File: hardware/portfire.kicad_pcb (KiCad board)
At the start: 2 copper layers, 100 x 100 mm, 200 parts, among them IC101 STM32F407VGT6TR, IC102 TPS62152, IC103 25AA02E48, IC104 ADP3335, IC105 SNx5176B, IC201 MAX5969x, IC202 KSZ8081RNA, IC203 MAX17503, IC301 TPS92512, J201 RJ45, J202 AUX POWER, P101 SWD_TC, P102 AUX_BUS_RX, P103 AUX_BUS_RX, P301 1, P302 2, P303 3, P304 4, P305 5, P306 6, P307 7, P308 8, P309 9, P310 10, P311 11, P312 12, P313 13, P314 14, P315 15, P316 16, P317 17, P318 18, P319 19, P320 20, P321 21, P322 22, P323 23, P324 24, P325 25, P326 26, P327 27, P328 28, P329 29, P330 30, Q301 NTR4501NT1G, Q302 NTR4501NT1G, Q303 NTR4501NT1G, Q304 NTR4501NT1G, Q305 NTR4501NT1G, Q306 NTR4501NT1G, Q307 NTR4501NT1G, Q308 NTR4501NT1G, Q309 NTR4501NT1G, Q310 NTR4501NT1G, Q311 NTR4501NT1G, Q312 NTR4501NT1G, Q313 NTR4501NT1G, Q314 NTR4501NT1G, Q315 NTR4501NT1G, Q316 NTR4501NT1G, Q317 NTR4501NT1G, Q318 NTR4501NT1G, Q319 NTR4501NT1G, Q320 NTR4501NT1G, Q321 NTR4501NT1G, Q322 NTR4501NT1G, Q323 NTR4501NT1G, Q324 NTR4501NT1G, Q325 NTR4501NT1G, Q326 NTR4501NT1G, Q327 NTR4501NT1G, Q328 NTR4501NT1G, Q329 NTR4501NT1G, Q330 NTR4501NT1G, T201 749010012A, X101 PART, X102 PART, X103 PART, X104 PART, Y101 26M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

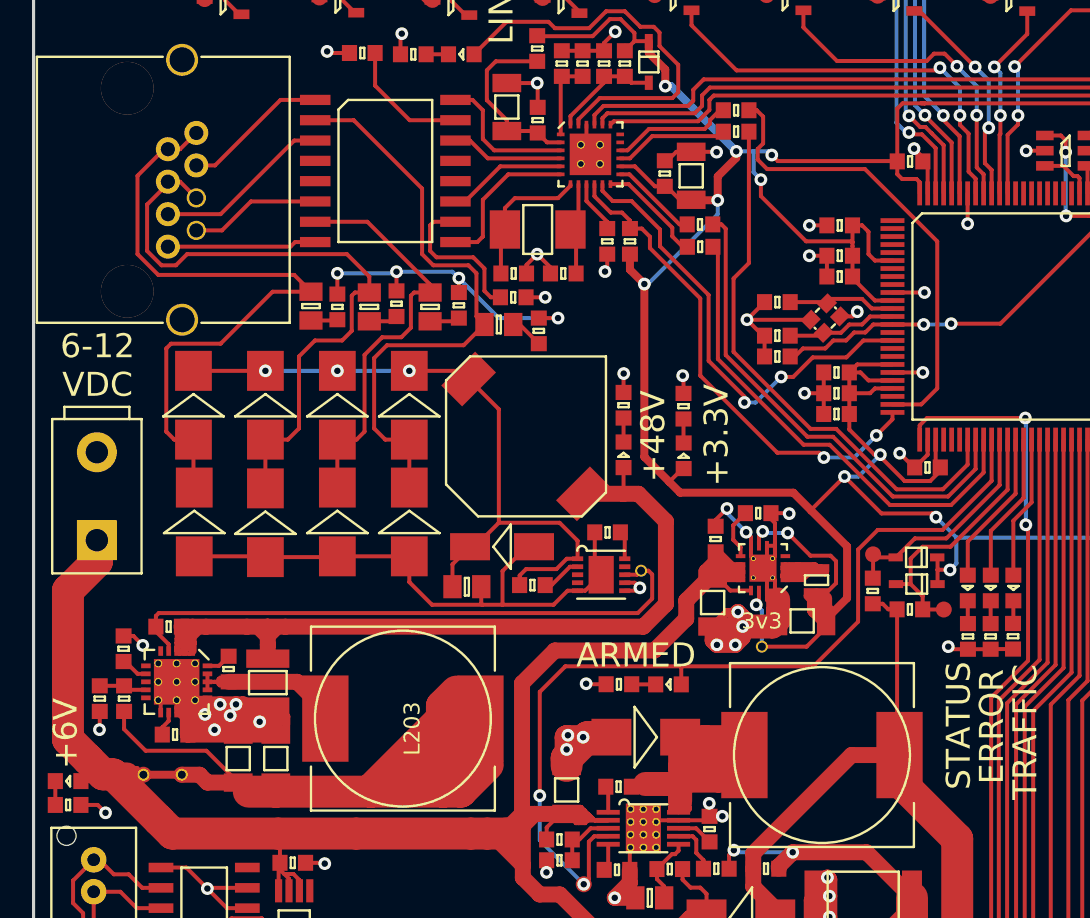
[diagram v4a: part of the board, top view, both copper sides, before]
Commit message: Shrank ethernet jack pins, beefed PD tracks
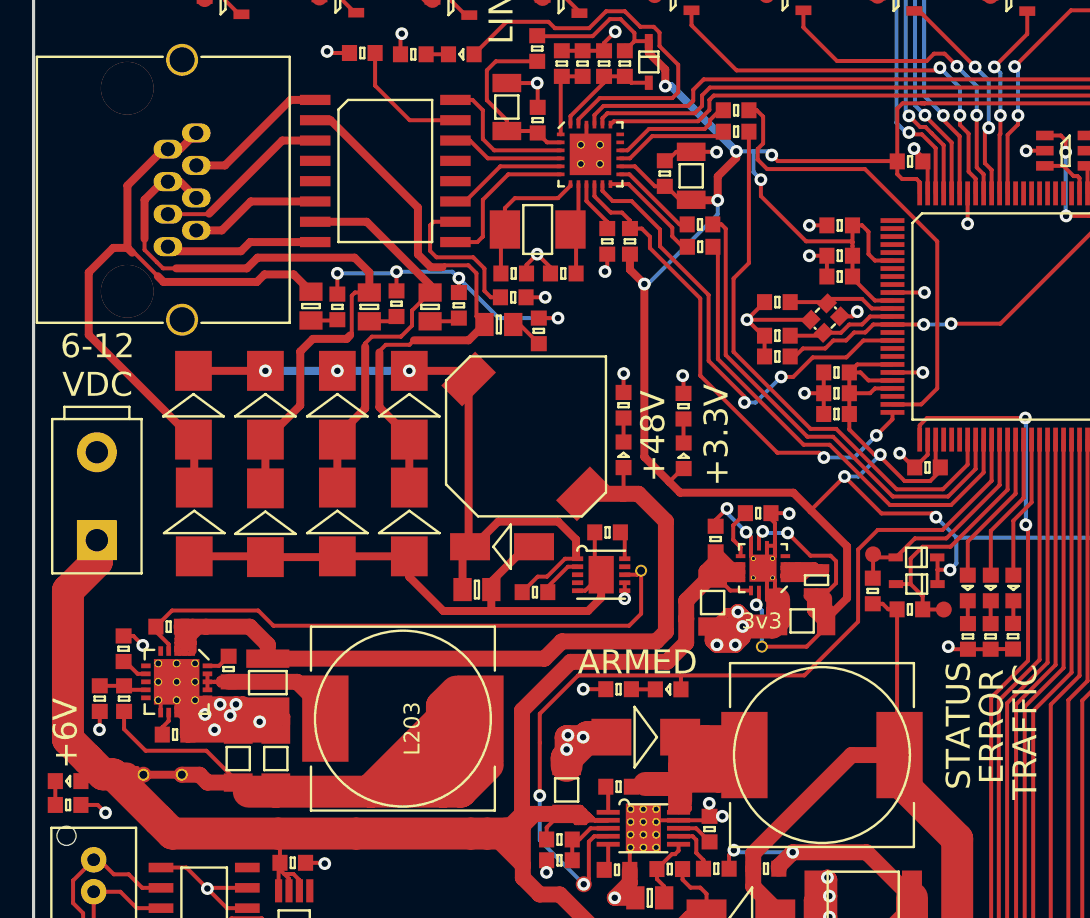
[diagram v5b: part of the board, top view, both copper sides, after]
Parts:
- moved C206 0.66 mm to (70.4, 98.8)
- moved R205 0.47 mm to (74.0, 99.0)
- moved R107 0.31 mm to (79.2, 105.1)
- moved D107 0.31 mm to (82.3, 105.1)
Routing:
- net Net-(C206-Pad2): track 41.0 -> 43.9 mm
- net +48V: track 60.5 -> 58.5 mm
- net /ethernet/VA1: track 37.5 -> 35.8 mm
- net Net-(C206-Pad1): track 44.3 -> 45.6 mm
- net /ARM: track 57.7 -> 56.6 mm
- net GND: track 214.8 -> 213.8 mm

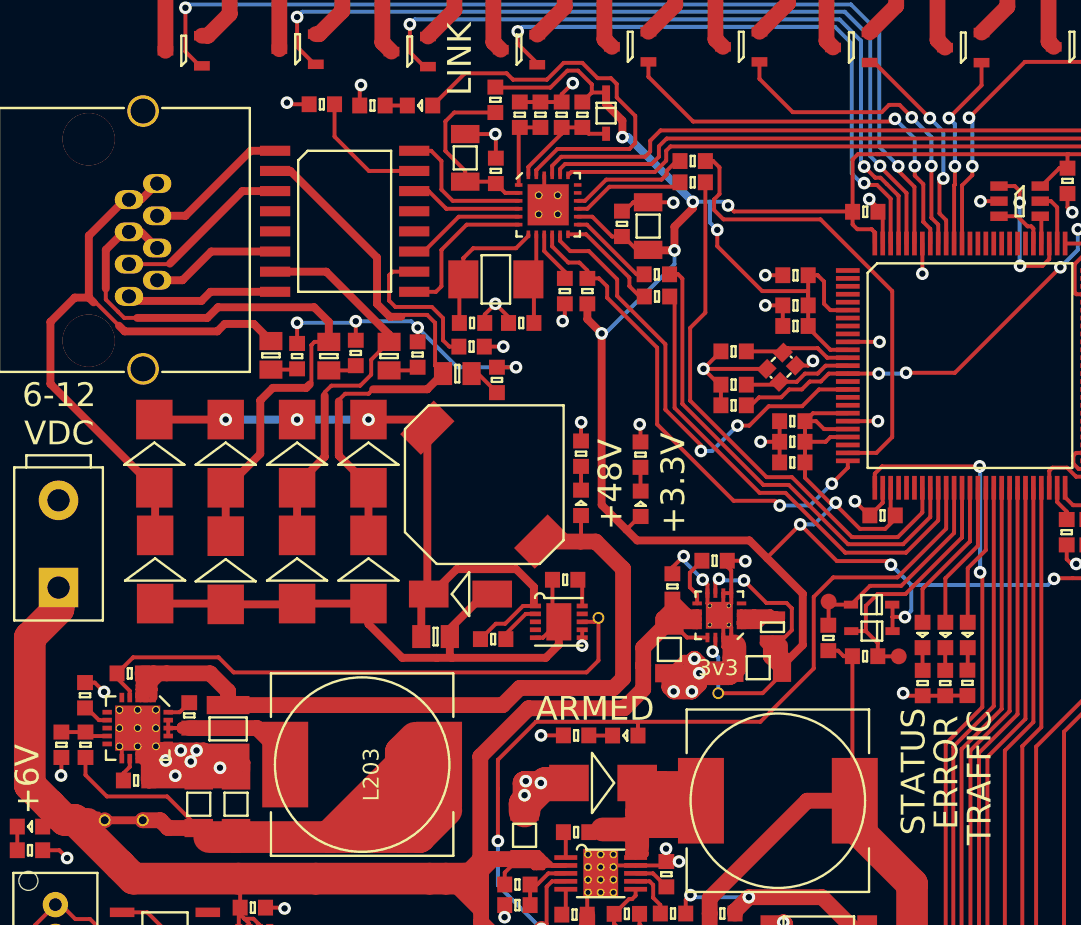
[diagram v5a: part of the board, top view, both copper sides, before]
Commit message: Fixed ERC and DRC issues
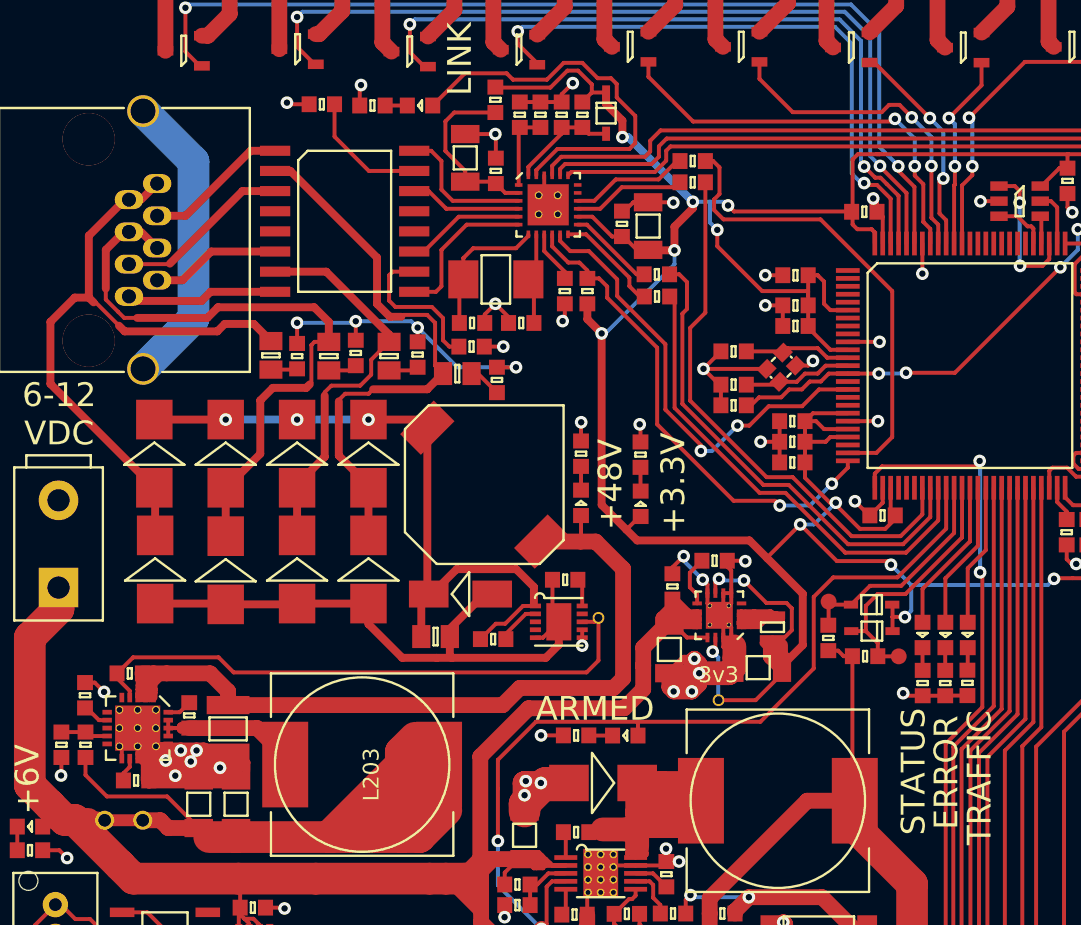
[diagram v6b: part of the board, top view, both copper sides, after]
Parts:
- removed TP205: 6V_SMPS, hardware:Test_point_mini
- removed TP206: 6V_BUS, hardware:Test_point_mini
- JP201: value Jumper_NC_Small -> Jumper_NO_Small; footprint hardware:jump_NC -> hardware:jump
- moved TP101 0.44 mm to (88.2, 102.8)
- moved C110 0.06 mm to (97.4, 72.0)
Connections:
- C222 pad 1: Net-(C222-Pad1) -> +6V
- C223 pad 1: Net-(C222-Pad1) -> +6V
- JP201 pad 1: Net-(C222-Pad1) -> +6V
- L203 pad 1: Net-(C222-Pad1) -> +6V
- R211 pad 1: Net-(C222-Pad1) -> +6V
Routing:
- net +6V: track 148.2 -> 203.4 mm
- net Net-(C222-Pad1): track 52.9 -> 0.00 mm
- net Net-(J201-Pad9): track 0.00 -> 18.9 mm
- net /AUX_BUS_RX: track 110.9 -> 111.5 mm
- net 3v3: track 230.6 -> 231.2 mm
- net +48V: track 58.5 -> 59.1 mm

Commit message: Made board beautiful
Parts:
- moved C101 4.52 mm to (86.5, 80.6)
- moved C102 4.52 mm to (107.5, 88.6)
- moved C111 4.52 mm to (108.8, 88.6)
- moved C112 4.52 mm to (112.5, 71.6)
- moved C117 4.52 mm to (88.1, 97.1)
- moved C123 4.52 mm to (86.5, 79.3)
- moved C204 4.52 mm to (69.1, 78.6)
- moved C211 4.52 mm to (73.1, 75.4)
- moved C214 4.52 mm to (81.1, 69.3)
- moved C217 4.52 mm to (69.6, 65.0)
- moved D303 4.52 mm to (84.2, 115.7)
- moved P101 4.52 mm to (112.8, 68.0)
- moved Q328 4.52 mm to (66.1, 58.3)
- moved R203 4.52 mm to (71.6, 79.0)
- moved R305 4.52 mm to (76.5, 112.7)
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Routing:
- net +48V: track 59.1 -> 58.5 mm
- net +6V: track 203.4 -> 204.0 mm
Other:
- board text added: "DAVID TURNER ADAM GREIG"
- board text added: "FIREWORK IGNITION SYSTEM"
- board text added: "ID:"
- board text added: "MAC:"
- board text added: "PORTFIRE"
- board text added: "REVISION 1 2016.10.13"
